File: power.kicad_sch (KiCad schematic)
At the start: 42 parts, among them U13 TPSM82903SISR, U14 TPSM82903SISR, U2 TPS546D24SRVFR

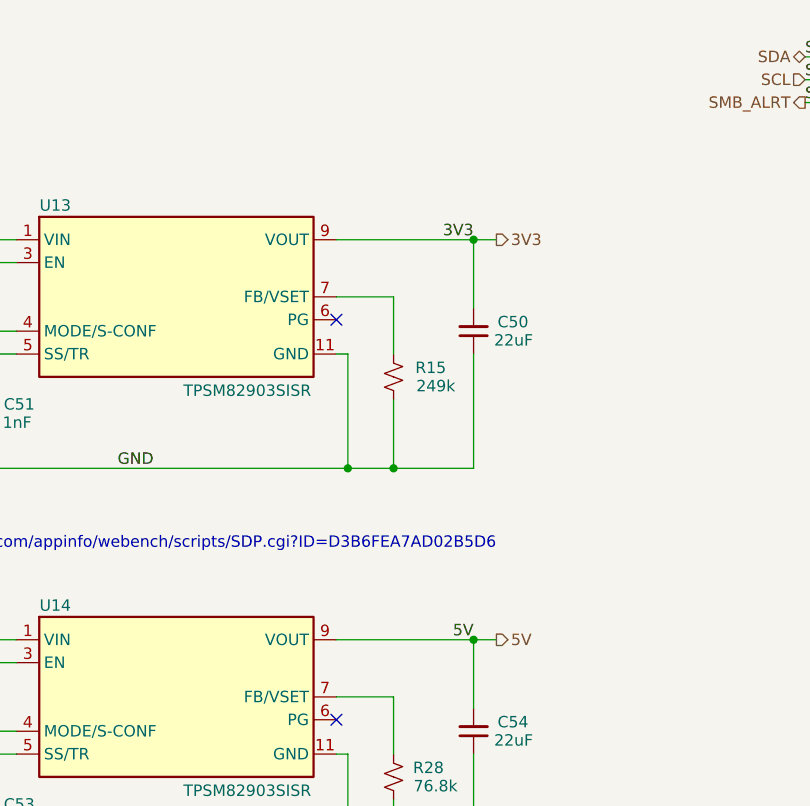
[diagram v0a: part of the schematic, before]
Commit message: Filled out the BOM and added missing DK part numbers. thanks Claude
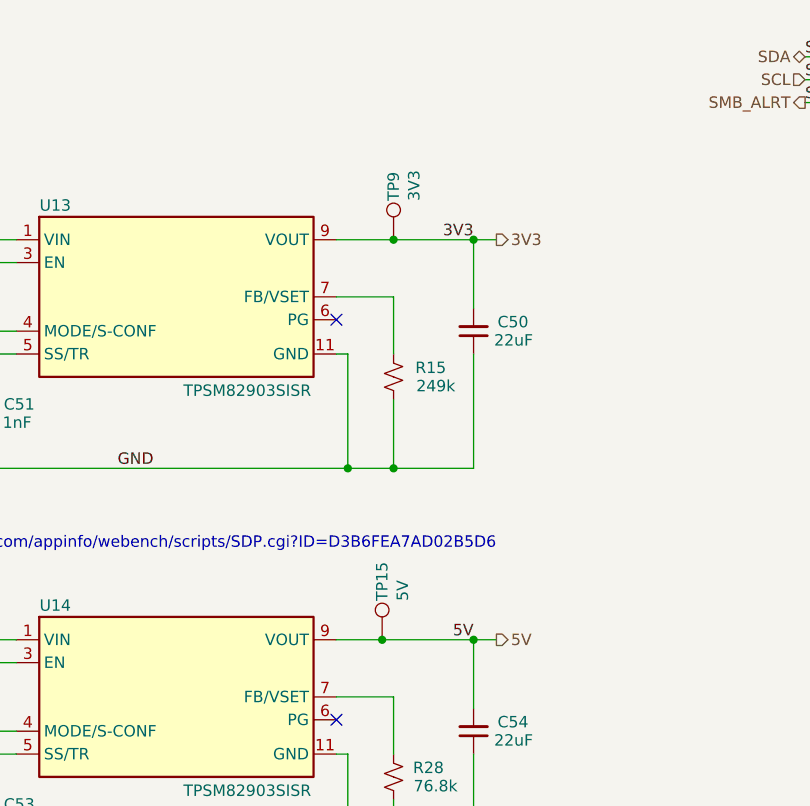
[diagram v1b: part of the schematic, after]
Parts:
- added TP15: 5V, bitaxe:TestPoint_Pad_D1.0mm, symbol Connector:TestPoint
- added TP9: 3V3, bitaxe:TestPoint_Pad_D1.0mm, symbol Connector:TestPoint
- C49, C52: DK (none) -> 445-14433-1-ND
- C50, C54: DK (none) -> 490-14659-1-ND
- C51, C53: DK (none) -> 490-6295-1-ND
- NT1: symbol Device:NetTie_2 -> bitaxe:NetTie_2
- R15: DK (none) -> 311-249KLRCT-ND; PARTNO (none) -> RC0402FR-07249KL
- R25, R27: DK (none) -> 311-40.2KLRCT-ND; PARTNO (none) -> RC0402FR-0740K2L
- R28: DK (none) -> YAG3230CT-ND; PARTNO (none) -> RC0402FR-0776K8L
- R6: DK RHM1KTR-ND -> RHM1KCT-ND
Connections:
- net 3V3: now also TP9.1
- net 5V: now also TP15.1

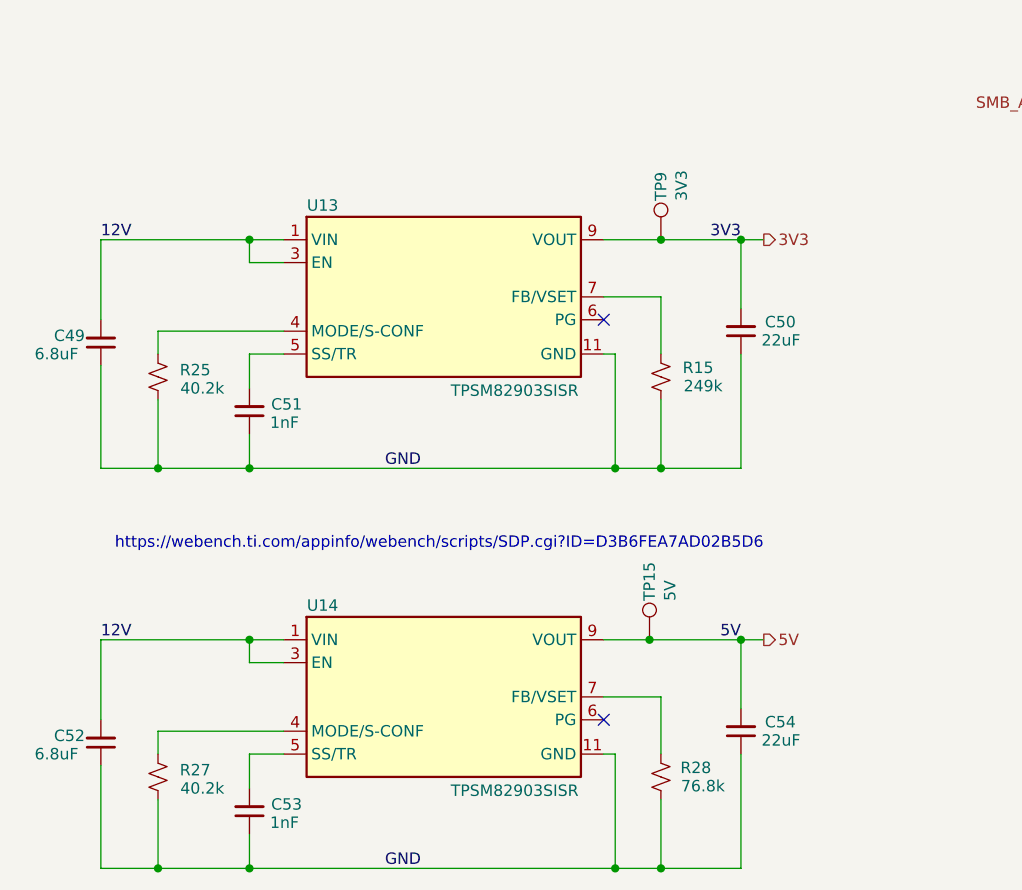
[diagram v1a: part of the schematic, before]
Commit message: switched back to TPS82130. added BOM partnumbers
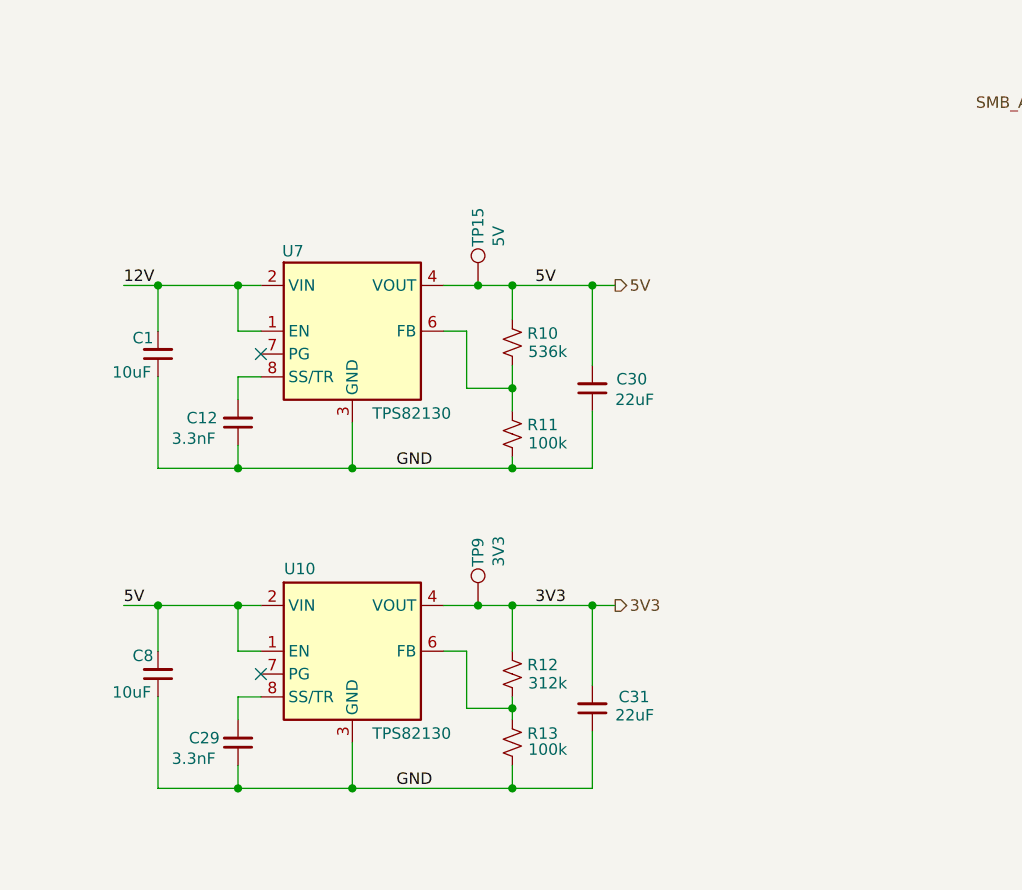
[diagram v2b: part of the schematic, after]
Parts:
- removed C49, C52: 6.8uF, Capacitor_SMD:C_0805_2012Metric, symbol Device:C_Small
- removed C50, C54: 22uF, Capacitor_SMD:C_0805_2012Metric, symbol Device:C_Small
- removed C51, C53: 1nF, Capacitor_SMD:C_0402_1005Metric, symbol Device:C_Small
- removed R15: 249k, Resistor_SMD:R_0402_1005Metric, symbol Device:R_Small_US
- removed R25, R27: 40.2k, Resistor_SMD:R_0402_1005Metric, symbol Device:R_Small_US
- removed R28: 76.8k, Resistor_SMD:R_0402_1005Metric, symbol Device:R_Small_US
- removed U13, U14: TPSM82903SISR, bitaxe:TPSM82903SISR, symbol bitaxe:TPSM82903SISR
- added C1, C8: 10uF, Capacitor_SMD:C_0805_2012Metric, symbol Device:C_Small
- added C12, C29: 3.3nF, Capacitor_SMD:C_0402_1005Metric, symbol Device:C_Small
- added C30, C31: 22uF, Capacitor_SMD:C_1206_3216Metric, symbol Device:C_Small
- added R10: 536k, Resistor_SMD:R_0402_1005Metric, symbol Device:R_Small_US
- added R11, R13: 100k, Resistor_SMD:R_0402_1005Metric, symbol Device:R_Small_US
- added R12: 312k, Resistor_SMD:R_0402_1005Metric, symbol Device:R_Small_US
- added U10, U7: TPS82130, bitaxe:Texas_SIL0008D_MicroSiP-8-1EP_2.8x3mm_P0.65mm_EP1.1x1.9mm_ThermalVias, symbol Regulator_Switching:TPS82130
- C15: LCSC (none) -> C52923
- C16: LCSC (none) -> C307331
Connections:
- net 12V: now also C1.2, U7.1 (EN), U7.2 (VIN)
- net 3V3: now also C31.2, R12.2, U10.4 (VOUT), U10.5 (VOUT)
- net 5V: now also C30.2, C8.2, R10.2, U10.1 (EN), U10.2 (VIN), U7.4 (VOUT), U7.5 (VOUT)
- net GND: now also C1.1, C12.1, C29.1, C30.1, C31.1, C8.1, R11.1, R13.1, U10.3 (GND), U10.9 (GND), U7.3 (GND), U7.9 (GND)
- new net: R12.1, R13.2, U10.6 (FB)
- new net: C12.2, U7.8 (SS/TR)
- new net: C29.2, U10.8 (SS/TR)
- new net: R10.1, R11.2, U7.6 (FB)
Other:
- note removed: "https://webench.ti.com/appinfo/webench/scripts/SDP.cgi?ID=D3B6FEA7AD02B5D6"
- moved on the sheet: TP15, TP9

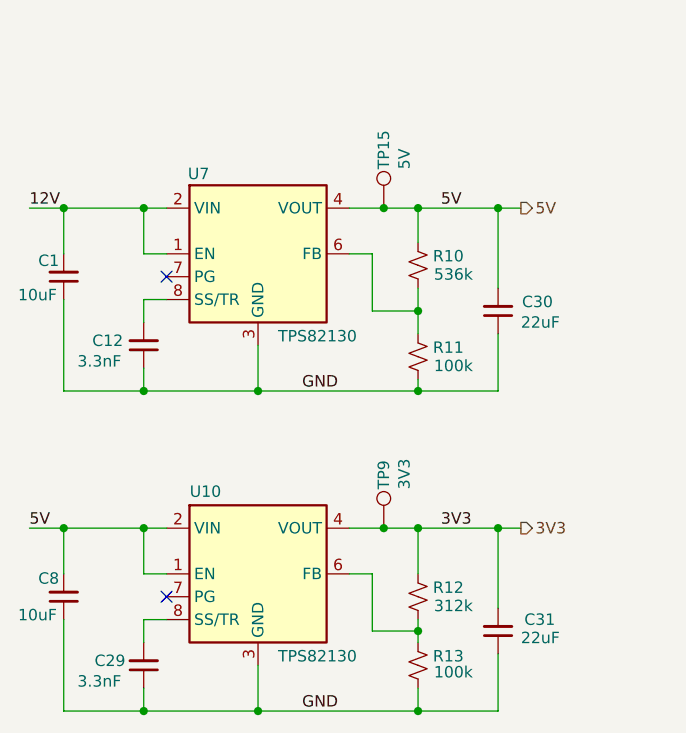
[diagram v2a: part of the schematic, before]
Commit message: fix TPS82130 symbols
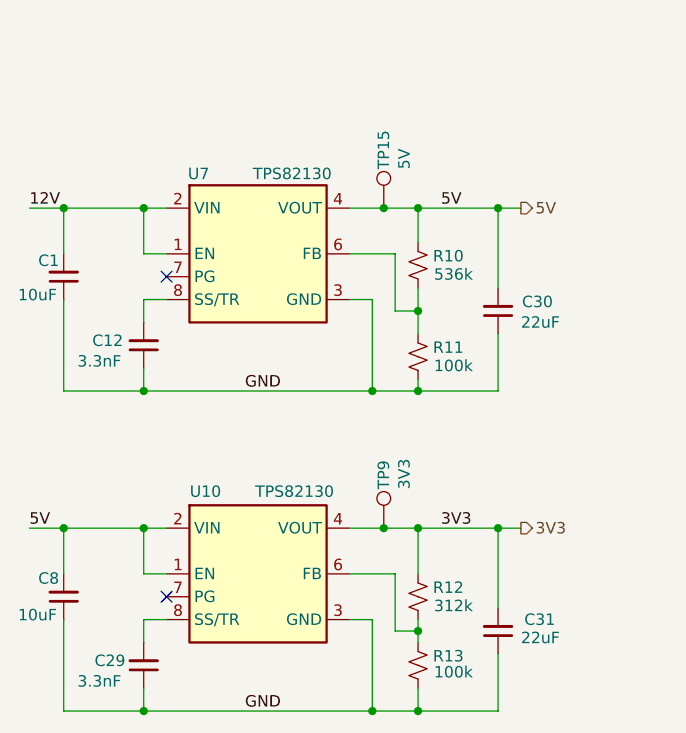
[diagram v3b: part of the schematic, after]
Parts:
- U10, U7: symbol Regulator_Switching:TPS82130 -> bitaxe:TPS82130
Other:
- moved on the sheet: U10, U7
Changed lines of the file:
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@@
 	)
 	(junction
+		(at 99.06 181.61)
+		(diameter 0)
+		(color 0 0 0 0)
+	)
+	(junction
 		(at 171.45 114.3)
 		(diameter 0)
@@
 	)
 	(junction
+		(at 99.06 217.17)
+		(diameter 0)
+		(color 0 0 0 0)
+	)
+	(junction
 		(at 212.09 102.87)
 		(diameter 0)
@@
 	)
 	(junction
-		(at 86.36 217.17)
-		(diameter 0)
-		(color 0 0 0 0)
-	)
-	(junction
 		(at 177.8 80.01)
 		(diameter 0)
@@
 		(color 0 0 0 0)
 	)
-	(junction
-		(at 86.36 181.61)
-		(diameter 0)
-		(color 0 0 0 0)
-	)
 	(no_connect
 		(at 181.61 125.73)
@@
 	(wire
 		(pts
+			(xy 96.52 171.45) (xy 99.06 171.45)
+		)
+		(stroke
+			(width 0)
+			(type default)
+		)
+	)
+	(wire
+		(pts
 			(xy 118.11 55.88) (xy 118.11 63.5)
 		)
@@
 	(wire
 		(pts
-			(xy 99.06 208.28) (xy 99.06 201.93)
+			(xy 101.6 208.28) (xy 101.6 201.93)
 		)
 		(stroke
@@
 	(wire
 		(pts
-			(xy 99.06 166.37) (xy 96.52 166.37)
+			(xy 101.6 166.37) (xy 96.52 166.37)
 		)
 		(stroke
@@
 	(wire
 		(pts
-			(xy 86.36 217.17) (xy 104.14 217.17)
+			(xy 73.66 217.17) (xy 99.06 217.17)
 		)
 		(stroke
@@
 	(wire
 		(pts
-			(xy 86.36 176.53) (xy 86.36 181.61)
-		)
-		(stroke
-			(width 0)
-			(type default)
-		)
-	)
-	(wire
-		(pts
 			(xy 171.45 55.88) (xy 177.8 55.88)
 		)
@@
 	(wire
 		(pts
-			(xy 99.06 208.28) (xy 104.14 208.28)
+			(xy 101.6 208.28) (xy 104.14 208.28)
 		)
 		(stroke
@@
 	(wire
 		(pts
-			(xy 86.36 212.09) (xy 86.36 217.17)
-		)
-		(stroke
-			(width 0)
-			(type default)
-		)
-	)
-	(wire
-		(pts
 			(xy 73.66 196.85) (xy 76.2 196.85)
 		)
@@
 	(wire
 		(pts
-			(xy 73.66 217.17) (xy 86.36 217.17)
-		)
-		(stroke
-			(width 0)
-			(type default)
-		)
-	)
-	(wire
-		(pts
 			(xy 212.09 97.79) (xy 212.09 99.06)
 		)
@@
 	(wire
 		(pts
+			(xy 96.52 207.01) (xy 99.06 207.01)
+		)
+		(stroke
+			(width 0)
+			(type default)
+		)
+	)
+	(wire
+		(pts
 			(xy 140.97 55.88) (xy 148.59 55.88)
 		)
@@
 	(wire
 		(pts
+			(xy 99.06 181.61) (xy 104.14 181.61)
+		)
+		(stroke
+			(width 0)
+			(type default)
+		)
+	)
+	(wire
+		(pts
 			(xy 212.09 99.06) (xy 214.63 99.06)
 		)
@@
 	(wire
 		(pts
-			(xy 99.06 201.93) (xy 96.52 201.93)
+			(xy 101.6 201.93) (xy 96.52 201.93)
 		)
 		(stroke
@@
 	(wire
 		(pts
+			(xy 99.06 171.45) (xy 99.06 181.61)
+		)
+		(stroke
+			(width 0)
+			(type default)
+		)
+	)
+	(wire
+		(pts
 			(xy 209.55 133.35) (xy 213.36 133.35)
 		)
@@
 	(wire
 		(pts
-			(xy 86.36 181.61) (xy 104.14 181.61)
+			(xy 73.66 181.61) (xy 99.06 181.61)
 		)
 		(stroke
@@
 	(wire
 		(pts
-			(xy 99.06 172.72) (xy 104.14 172.72)
+			(xy 101.6 172.72) (xy 104.14 172.72)
 		)
 		(stroke
@@
 	(wire
 		(pts
-			(xy 73.66 181.61) (xy 86.36 181.61)
-		)
-		(stroke
-			(width 0)
-			(type default)
-		)
-	)
-	(wire
-		(pts
 			(xy 212.09 100.33) (xy 212.09 102.87)
 		)
@@
 	(wire
 		(pts
+			(xy 99.06 217.17) (xy 104.14 217.17)
+		)
+		(stroke
+			(width 0)
+			(type default)
+		)
+	)
+	(wire
+		(pts
 			(xy 125.73 55.88) (xy 133.35 55.88)
 		)
@@
 	(wire
 		(pts
-			(xy 99.06 172.72) (xy 99.06 166.37)
+			(xy 101.6 172.72) (xy 101.6 166.37)
 		)
 		(stroke
@@
 	(wire
 		(pts
+			(xy 99.06 207.01) (xy 99.06 217.17)
+		)
+		(stroke
+			(width 0)
+			(type default)
+		)
+	)
+	(wire
+		(pts
 			(xy 64.77 161.29) (xy 73.66 161.29)
 		)
@@
 	)
 	(label "GND"
-		(at 95.25 181.61 180)
+		(at 88.9 181.61 180)
 		(effects
 			(font
@@
 	)
 	(label "GND"
-		(at 95.25 217.17 180)
+		(at 88.9 217.17 180)
 		(effects
 			(font
@@
 	)
 	(symbol
-		(lib_id "Regulator_Switching:TPS82130")
+		(lib_id "bitaxe:TPS82130")
 		(at 86.36 201.93 0)
 		(unit 1)
@@
 		)
 		(property "Value" "TPS82130"
-			(at 92.964 211.074 0)
+			(at 90.424 192.786 0)
 			(effects
 				(font
@@
 		)
 		(property "Description" "17V Input 3A Step-Down Converter MicroSiP Module with Integrated Inductor, μSiL-8"
-			(at 86.36 201.93 0)
+			(at 87.122 226.06 0)
 			(effects
 				(font
@@
 		)
 		(property "DK" "296-47436-1-ND"
-			(at 86.36 201.93 0)
+			(at 87.376 228.346 0)
 			(effects
 				(font
@@
 		)
 		(property "PARTNO" "TPS82130SILR"
-			(at 86.36 201.93 0)
+			(at 86.36 230.378 0)
 			(effects
 				(font
@@
 		)
 		(property "LCSC" "C473914"
-			(at 86.36 201.93 0)
+			(at 86.36 232.664 0)
 			(effects
 				(font
@@
 		)
 		(property "ME" "595-TPS82130SILR"
-			(at 86.36 201.93 0)
+			(at 86.868 224.028 0)
 			(effects
 				(font
@@
 	)
 	(symbol
-		(lib_id "Regulator_Switching:TPS82130")
+		(lib_id "bitaxe:TPS82130")
 		(at 86.36 166.37 0)
 		(unit 1)
@@
 		)
 		(property "Value" "TPS82130"
-			(at 92.964 175.514 0)
+			(at 90.17 157.48 0)
 			(effects
 				(font
@@
 		)
 		(property "Description" "17V Input 3A Step-Down Converter MicroSiP Module with Integrated Inductor, μSiL-8"
-			(at 86.36 166.37 0)
+			(at 87.122 190.5 0)
 			(effects
 				(font
@@
 		)
 		(property "DK" "296-47436-1-ND"
-			(at 86.36 166.37 0)
+			(at 87.376 192.786 0)
 			(effects
 				(font
@@
 		)
 		(property "PARTNO" "TPS82130SILR"
-			(at 86.36 166.37 0)
+			(at 86.36 194.818 0)
 			(effects
 				(font
@@
 		)
 		(property "ME" "595-TPS82130SILR"
-			(at 86.36 166.37 0)
+			(at 86.868 188.468 0)
 			(effects
 				(font
@@
 		)
 		(property "LCSC" "C473914"
-			(at 86.36 166.37 0)
+			(at 86.36 197.104 0)
 			(effects
 				(font

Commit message: add missing cad files. bump to kicad v10
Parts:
- removed C2: 27uF, Capacitor_SMD:CP_Elec_5x5.9, symbol Device:C_Polarized_Small_US
- added C2: 22uF, Capacitor_SMD:C_1206_3216Metric, symbol Device:C_Small
- C10, C9: DK 587-2984-1-ND -> 1276-1184-1-ND; PARTNO TMK107B7105KA-T -> CL10B105KA8NNNC
- R12: value 312k -> 309k; DK 13-RC0402FR-1312KLCT-ND -> (none); PARTNO RC0402FR-1312KL -> (none)
- U2: DK 296-TPS546D24ARVFRCT-ND -> 296-TPS546D24SRVFRCT-ND; PARTNO TPS546D24ARVFR -> TPS546D24SRVFR
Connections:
- net 12V: now also C2.1
- net GND: now also C2.2

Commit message: minor silkscreen fixes. changed C1, C8 to 0805
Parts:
- C1, C8: footprint Capacitor_SMD:C_0805_2012Metric -> Capacitor_SMD:C_0603_1608Metric; DK 1276-6454-1-ND -> 490-18214-1-ND; PARTNO CL21A106KAYNNNG -> GRM188R61E106KA73D
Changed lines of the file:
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@@
 			)
 		)
-		(property "Footprint" "Capacitor_SMD:C_0805_2012Metric"
+		(property "Footprint" "Capacitor_SMD:C_0603_1608Metric"
 			(at 64.77 204.47 0)
 			(hide yes)
@@
 			)
 		)
-		(property "PARTNO" "CL21A106KAYNNNG"
+		(property "PARTNO" "GRM188R61E106KA73D"
 			(at 64.77 204.47 90)
 			(hide yes)
@@
 			)
 		)
-		(property "DK" "1276-6454-1-ND"
+		(property "DK" "490-18214-1-ND"
 			(at 64.77 204.47 90)
 			(hide yes)
@@
 			)
 		)
-		(property "Footprint" "Capacitor_SMD:C_0805_2012Metric"
+		(property "Footprint" "Capacitor_SMD:C_0603_1608Metric"
 			(at 64.77 168.91 0)
 			(hide yes)
@@
 			)
 		)
-		(property "PARTNO" "CL21A106KAYNNNG"
+		(property "PARTNO" "GRM188R61E106KA73D"
 			(at 64.77 168.91 90)
 			(hide yes)
@@
 			)
 		)
-		(property "DK" "1276-6454-1-ND"
+		(property "DK" "490-18214-1-ND"
 			(at 64.77 168.91 90)
 			(hide yes)
